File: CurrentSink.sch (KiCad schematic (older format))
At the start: 12 parts

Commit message: Updating the Schematic
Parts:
- removed U?: MIC5205-2.5YM5, Package_TO_SOT_SMD:SOT-23-5, symbol Regulator_Linear:MIC5205-2.5YM5
- added R? (x2): 10K, symbol Device:R
- added U?: TPS7A2401, symbol CurrentSink:TPS7A2401
- C?: value C -> 10uF
- C?: value C -> 1uF
- Q?: value Q_NMOS_DSG -> STP55NF06L; footprint (none) -> Package_TO_SOT_THT:TO-220-3_Vertical; MPN (none) -> STP55NF06L
- R?: value R -> 0.1
- U?: value MCP6002-xSN -> MCP6002; footprint (none) -> Package_SO:SOIC-8_3.9x4.9mm_P1.27mm; MPN (none) -> MCP6002T-I/SN
- U? (x2): value MCP6002-xSN -> MCP6002; footprint (none) -> Package_SO:SOIC-8_3.9x4.9mm_P1.27mm
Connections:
- wire segments 46 -> 57
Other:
- moved on the sheet: C?, U?C
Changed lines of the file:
@@
 P 5000 2650
 F 0 "U?" H 5000 3017 50  0000 C CNN
-F 1 "MCP6002-xSN" H 5000 2926 50  0000 C CNN
-F 2 "" H 5000 2650 50  0001 C CNN
+F 1 "MCP6002" H 5000 2926 50  0000 C CNN
+F 2 "Package_SO:SOIC-8_3.9x4.9mm_P1.27mm" H 5000 2650 50  0001 C CNN
 F 3 "http://ww1.microchip.com/downloads/en/DeviceDoc/21733j.pdf" H 5000 2650 50  0001 C CNN
+F 4 "MCP6002T-I/SN" H 5000 2650 50  0001 C CNN "MPN"
 	1    5000 2650
 	1    0    0    -1
@@
 L Amplifier_Operational:MCP6002-xSN U?
 U 3 1 6008AAAD
-P 8700 1450
-F 0 "U?" H 8658 1496 50  0000 L CNN
-F 1 "MCP6002-xSN" H 8658 1405 50  0000 L CNN
-F 2 "" H 8700 1450 50  0001 C CNN
-F 3 "http://ww1.microchip.com/downloads/en/DeviceDoc/21733j.pdf" H 8700 1450 50  0001 C CNN
-	3    8700 1450
+P 9100 1500
+F 0 "U?" H 9058 1546 50  0000 L CNN
+F 1 "MCP6002" H 9058 1455 50  0000 L CNN
+F 2 "Package_SO:SOIC-8_3.9x4.9mm_P1.27mm" H 9100 1500 50  0001 C CNN
+F 3 "http://ww1.microchip.com/downloads/en/DeviceDoc/21733j.pdf" H 9100 1500 50  0001 C CNN
+	3    9100 1500
 	1    0    0    -1
 $EndComp
@@
 P 2500 2850
 F 0 "U?" H 2500 3217 50  0000 C CNN
-F 1 "MCP6002-xSN" H 2500 3126 50  0000 C CNN
-F 2 "" H 2500 2850 50  0001 C CNN
+F 1 "MCP6002" H 2500 3126 50  0000 C CNN
+F 2 "Package_SO:SOIC-8_3.9x4.9mm_P1.27mm" H 2500 2850 50  0001 C CNN
 F 3 "http://ww1.microchip.com/downloads/en/DeviceDoc/21733j.pdf" H 2500 2850 50  0001 C CNN
 	2    2500 2850
-	1    0    0    -1
-$EndComp
-$Comp
-L Regulator_Linear:MIC5205-2.5YM5 U?
-U 1 1 60092225
-P 7450 1100
-F 0 "U?" H 7450 1442 50  0000 C CNN
-F 1 "MIC5205-2.5YM5" H 7450 1351 50  0000 C CNN
-F 2 "Package_TO_SOT_SMD:SOT-23-5" H 7450 1425 50  0001 C CNN
-F 3 "http://ww1.microchip.com/downloads/en/DeviceDoc/20005785A.pdf" H 7450 1100 50  0001 C CNN
-	1    7450 1100
 	1    0    0    -1
 $EndComp
@@
 P 6100 2650
 F 0 "Q?" H 6304 2696 50  0000 L CNN
-F 1 "Q_NMOS_DSG" H 6304 2605 50  0000 L CNN
-F 2 "" H 6300 2750 50  0001 C CNN
-F 3 "~" H 6100 2650 50  0001 C CNN
+F 1 "STP55NF06L" H 6304 2605 50  0000 L CNN
+F 2 "Package_TO_SOT_THT:TO-220-3_Vertical" H 6300 2750 50  0001 C CNN
+F 3 "https://www.st.com/content/ccc/resource/technical/document/datasheet/49/c5/a8/71/93/60/4f/86/CD00002690.pdf/files/CD00002690.pdf/jcr:content/translations/en.CD00002690.pdf" H 6100 2650 50  0001 C CNN
+F 4 "STP55NF06L" H 6100 2650 50  0001 C CNN "MPN"
 	1    6100 2650
 	1    0    0    -1
@@
 P 6200 3500
 F 0 "R?" H 6270 3546 50  0000 L CNN
-F 1 "R" H 6270 3455 50  0000 L CNN
+F 1 "0.1" H 6270 3455 50  0000 L CNN
 F 2 "" V 6130 3500 50  0001 C CNN
 F 3 "~" H 6200 3500 50  0001 C CNN
@@
 L Device:C C?
 U 1 1 600F940B
-P 8100 1300
-F 0 "C?" H 8215 1346 50  0000 L CNN
-F 1 "C" H 8215 1255 50  0000 L CNN
-F 2 "" H 8138 1150 50  0001 C CNN
-F 3 "~" H 8100 1300 50  0001 C CNN
-	1    8100 1300
+P 8550 1400
+F 0 "C?" H 8665 1446 50  0000 L CNN
+F 1 "10uF" H 8665 1355 50  0000 L CNN
+F 2 "" H 8588 1250 50  0001 C CNN
+F 3 "~" H 8550 1400 50  0001 C CNN
+	1    8550 1400
 	1    0    0    -1
 $EndComp
@@
 L Device:C C?
 U 1 1 600F9C77
-P 6750 1300
-F 0 "C?" H 6865 1346 50  0000 L CNN
-F 1 "C" H 6865 1255 50  0000 L CNN
-F 2 "" H 6788 1150 50  0001 C CNN
-F 3 "~" H 6750 1300 50  0001 C CNN
-	1    6750 1300
-	1    0    0    -1
-$EndComp
-Wire Wire Line
-	7750 1000 8100 1000
-Wire Wire Line
-	8600 1000 8600 1150
-Wire Wire Line
-	8100 1150 8100 1000
-Connection ~ 8100 1000
-Wire Wire Line
-	8100 1000 8600 1000
-Wire Wire Line
-	6750 1150 6750 1000
-Wire Wire Line
-	6750 1000 7150 1000
-Wire Wire Line
-	6750 1450 6750 1850
-Wire Wire Line
-	6750 1850 7450 1850
-Wire Wire Line
-	8600 1850 8600 1750
-Wire Wire Line
-	8100 1450 8100 1850
-Connection ~ 8100 1850
-Wire Wire Line
-	8100 1850 8600 1850
-Wire Wire Line
-	7450 1400 7450 1850
-Connection ~ 7450 1850
-Wire Wire Line
-	7450 1850 7750 1850
+P 6650 1400
+F 0 "C?" H 6765 1446 50  0000 L CNN
+F 1 "1uF" H 6765 1355 50  0000 L CNN
+F 2 "" H 6688 1250 50  0001 C CNN
+F 3 "~" H 6650 1400 50  0001 C CNN
+	1    6650 1400
+	1    0    0    -1
+$EndComp
 $Comp
 L power:GND #PWR?
 U 1 1 601192B6
-P 7750 2000
-F 0 "#PWR?" H 7750 1750 50  0001 C CNN
-F 1 "GND" H 7755 1827 50  0000 C CNN
-F 2 "" H 7750 2000 50  0001 C CNN
-F 3 "" H 7750 2000 50  0001 C CNN
-	1    7750 2000
-	1    0    0    -1
-$EndComp
-Wire Wire Line
-	7750 2000 7750 1850
-Connection ~ 7750 1850
-Wire Wire Line
-	7750 1850 8100 1850
+P 7500 2050
+F 0 "#PWR?" H 7500 1800 50  0001 C CNN
+F 1 "GND" H 7505 1877 50  0000 C CNN
+F 2 "" H 7500 2050 50  0001 C CNN
+F 3 "" H 7500 2050 50  0001 C CNN
+	1    7500 2050
+	1    0    0    -1
+$EndComp
 $Comp
 L Device:R_POT RV?
@@
 	6200 3650 6200 3950
 Wire Wire Line
-	6200 3950 4100 3950
+	6200 3950 5200 3950
 Text GLabel 4100 1850 1    50   Input ~ 0
 Vload
-Text GLabel 6350 1000 0    50   Input ~ 0
+Text GLabel 6500 950  0    50   Input ~ 0
 Vload
 Wire Wire Line
-	6350 1000 6750 1000
-Connection ~ 6750 1000
-Wire Wire Line
 	4100 1850 4100 2500
-Text GLabel 8850 1000 2    50   Input ~ 0
+Text GLabel 9250 950  2    50   Input ~ 0
 Vcc
-Wire Wire Line
-	8850 1000 8600 1000
-Connection ~ 8600 1000
 Text GLabel 1850 1950 1    50   Input ~ 0
 Vcc
@@
 	1    0    0    -1
 $EndComp
+$Comp
+L power:GND #PWR?
+U 1 1 600A09A2
+P 5200 4050
+F 0 "#PWR?" H 5200 3800 50  0001 C CNN
+F 1 "GND" H 5205 3877 50  0000 C CNN
+F 2 "" H 5200 4050 50  0001 C CNN
+F 3 "" H 5200 4050 50  0001 C CNN
+	1    5200 4050
+	1    0    0    -1
+$EndComp
+Wire Wire Line
+	5200 4050 5200 3950
+Connection ~ 5200 3950
+Wire Wire Line
+	5200 3950 4100 3950
+$Comp
+L CurrentSink:TPS7A2401 U?
+U 1 1 600F4C8B
+P 7500 1300
+F 0 "U?" H 7500 1915 50  0000 C CNN
+F 1 "TPS7A2401" H 7500 1824 50  0000 C CNN
+F 2 "" H 7500 1300 50  0001 C CNN
+F 3 "" H 7500 1300 50  0001 C CNN
+	1    7500 1300
+	1    0    0    -1
+$EndComp
+Wire Wire Line
+	6500 950  6650 950
+Wire Wire Line
+	6650 1250 6650 950
+Connection ~ 6650 950
+Wire Wire Line
+	6650 950  6900 950
+Wire Wire Line
+	7000 1100 6900 1100
+Wire Wire Line
+	6900 1100 6900 950
+Connection ~ 6900 950
+Wire Wire Line
+	6900 950  7000 950
+Wire Wire Line
+	6650 1550 6650 2000
+Wire Wire Line
+	6650 2000 7500 2000
+Wire Wire Line
+	7500 2000 7500 1850
+Wire Wire Line
+	7500 2050 7500 2000
+Connection ~ 7500 2000
+Wire Wire Line
+	8000 950  8200 950
+Wire Wire Line
+	9000 1200 9000 950
+Connection ~ 9000 950
+Wire Wire Line
+	9000 950  9250 950
+Wire Wire Line
+	8550 1250 8550 950
+Connection ~ 8550 950
+Wire Wire Line
+	8550 950  9000 950
+$Comp
+L Device:R R?
+U 1 1 600FFFE5
+P 8200 1150
+F 0 "R?" H 8270 1196 50  0000 L CNN
+F 1 "10K" H 8270 1105 50  0000 L CNN
+F 2 "" V 8130 1150 50  0001 C CNN
+F 3 "~" H 8200 1150 50  0001 C CNN
+	1    8200 1150
+	1    0    0    -1
+$EndComp
+$Comp
+L Device:R R?
+U 1 1 601007C4
+P 8200 1650
+F 0 "R?" H 8270 1696 50  0000 L CNN
+F 1 "10K" H 8270 1605 50  0000 L CNN
+F 2 "" V 8130 1650 50  0001 C CNN
+F 3 "~" H 8200 1650 50  0001 C CNN
+	1    8200 1650
+	1    0    0    -1
+$EndComp
+Wire Wire Line
+	8200 1000 8200 950
+Connection ~ 8200 950
+Wire Wire Line
+	8200 950  8550 950
+Wire Wire Line
+	8200 1300 8200 1400
+Wire Wire Line
+	8200 1800 8200 2000
+Wire Wire Line
+	8200 2000 7500 2000
+Wire Wire Line
+	8000 1400 8200 1400
+Connection ~ 8200 1400
+Wire Wire Line
+	8200 1400 8200 1500
+Wire Wire Line
+	9000 1800 9000 2000
+Wire Wire Line
+	9000 2000 8550 2000
+Connection ~ 8200 2000
+Wire Wire Line
+	8550 1550 8550 2000
+Connection ~ 8550 2000
+Wire Wire Line
+	8550 2000 8200 2000
 $EndSCHEMATC

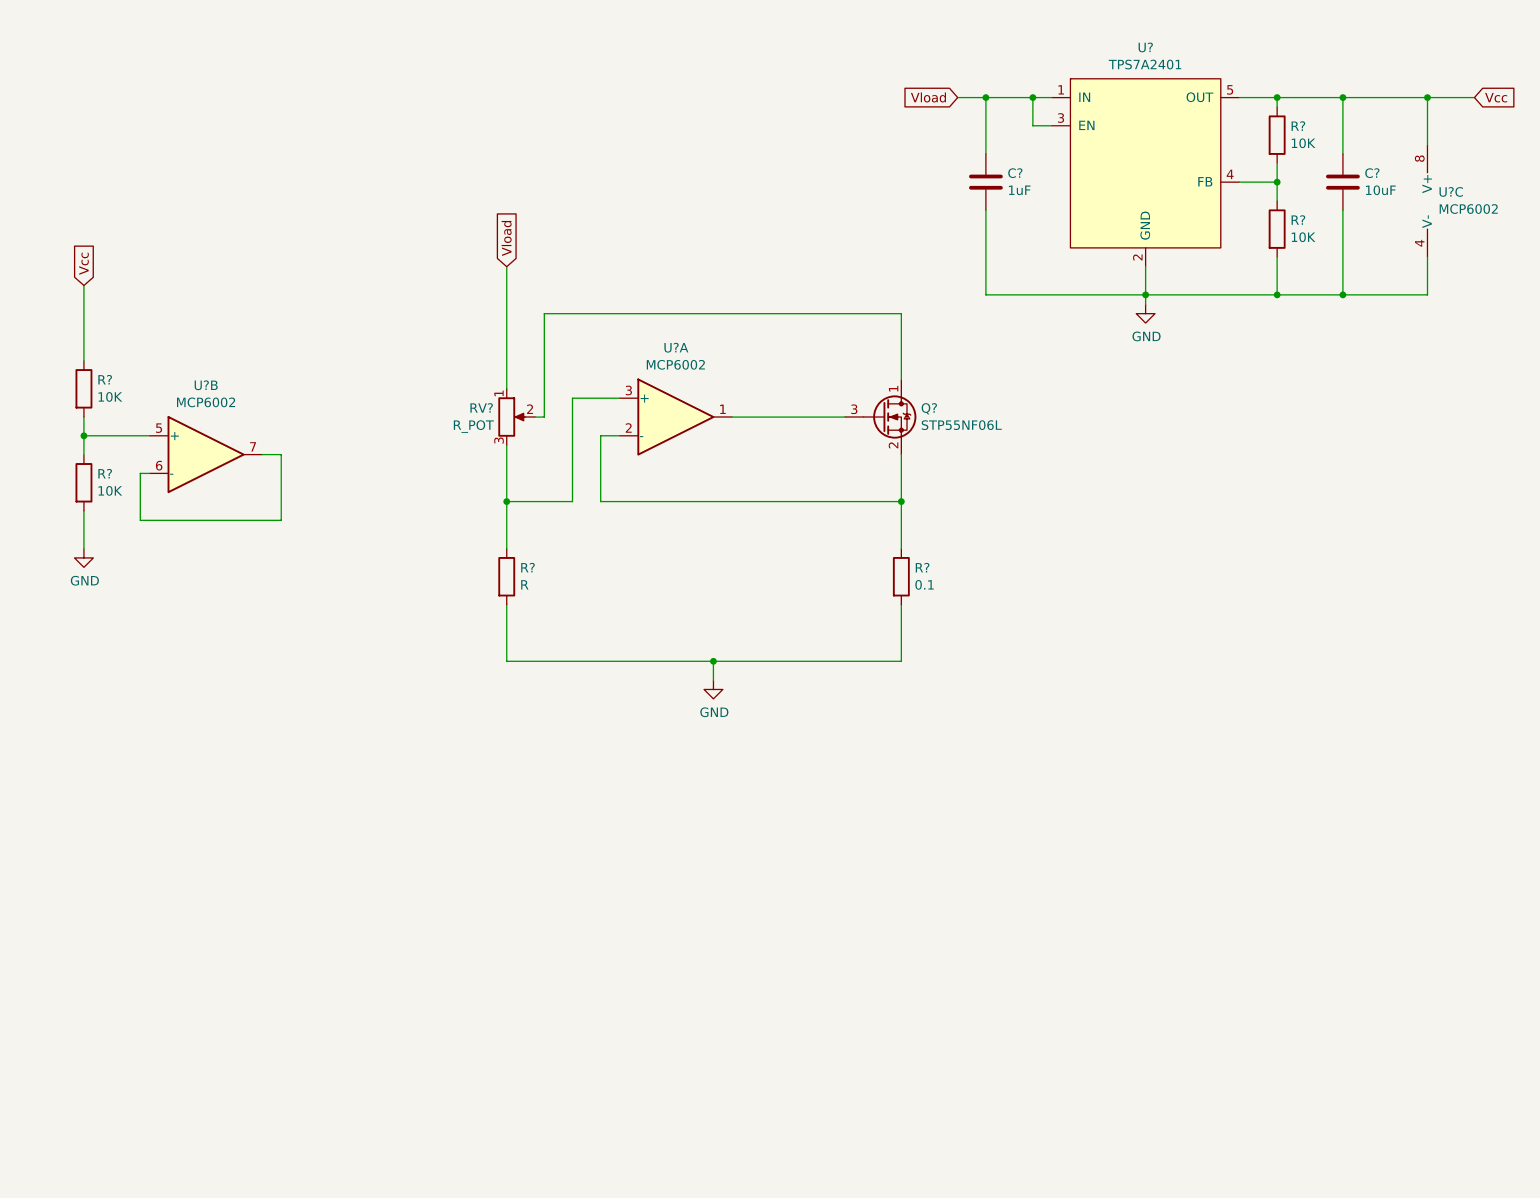
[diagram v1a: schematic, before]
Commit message: Schematic final version and preliminary footprints
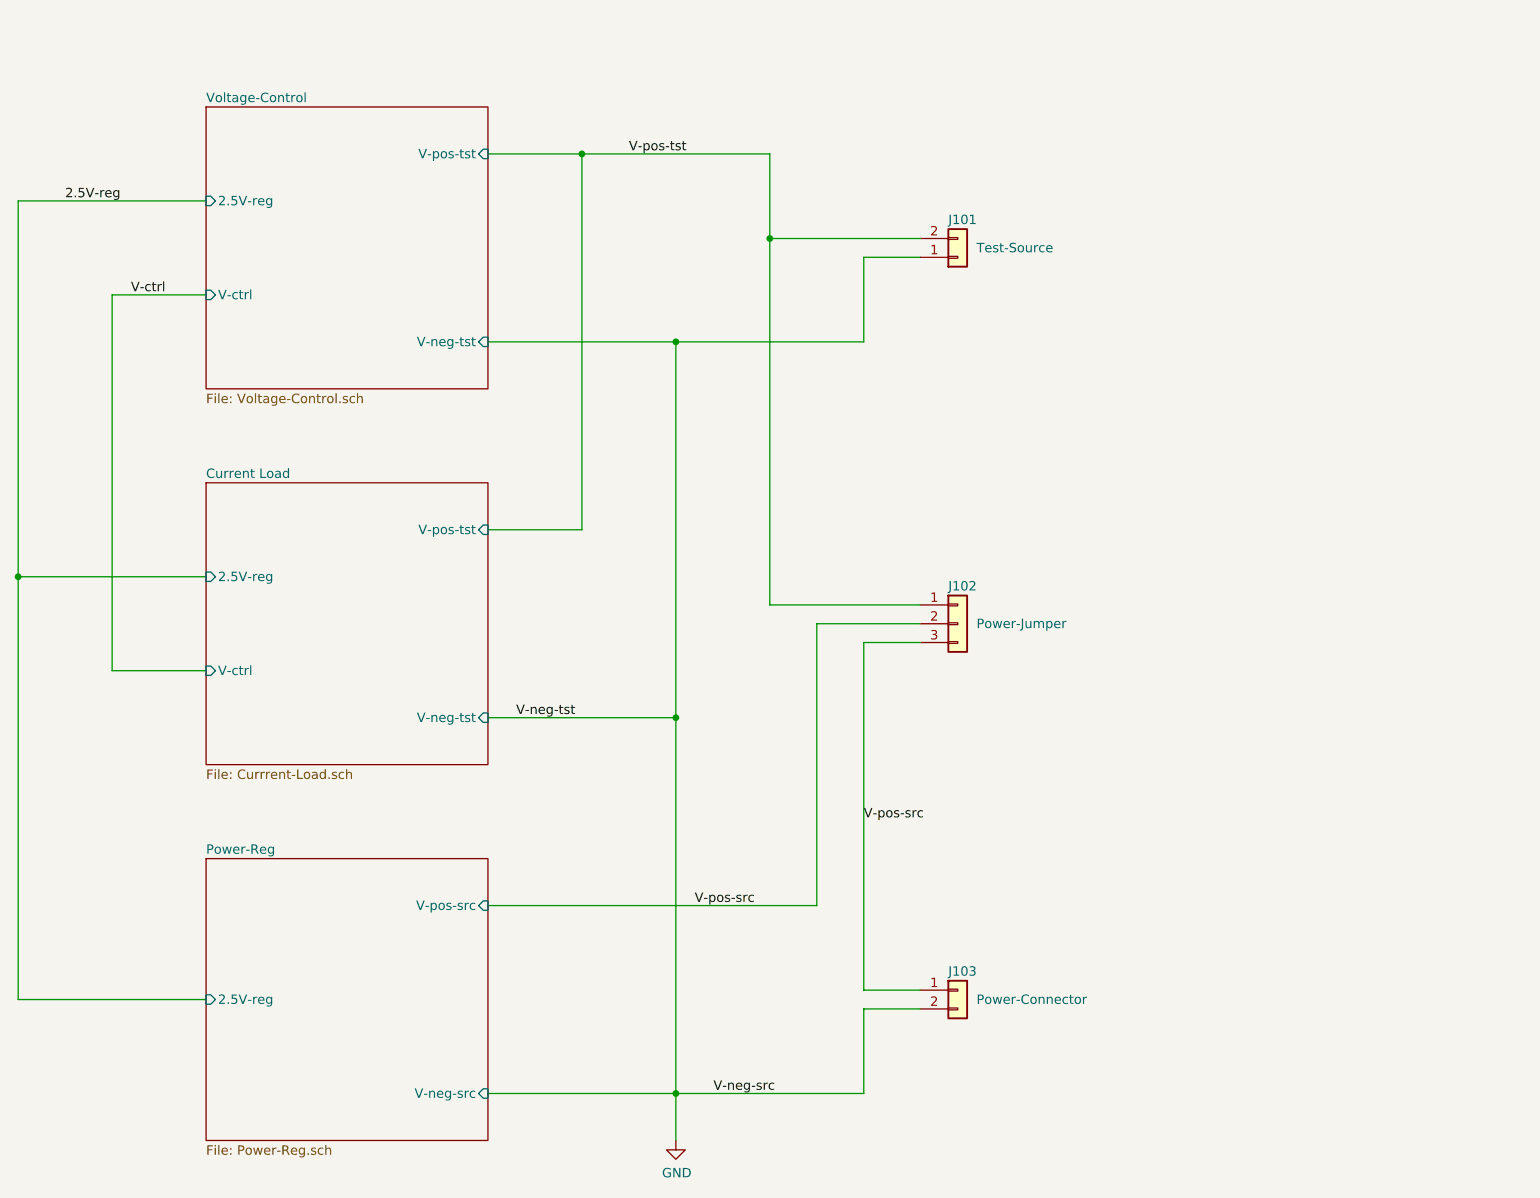
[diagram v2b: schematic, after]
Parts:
- removed C?: 10uF, symbol Device:C
- removed C?: 1uF, symbol Device:C
- removed Q?: STP55NF06L, Package_TO_SOT_THT:TO-220-3_Vertical, symbol Device:Q_NMOS_DSG
- removed R?: 0.1, symbol Device:R
- removed R?: R, symbol Device:R
- removed R? (x4): 10K, symbol Device:R
- removed RV?: R_POT, symbol Device:R_POT
- removed U? (x3): MCP6002, Package_SO:SOIC-8_3.9x4.9mm_P1.27mm, symbol Amplifier_Operational:MCP6002-xSN
- removed U?: TPS7A2401, symbol CurrentSink:TPS7A2401
- added J101: Test-Source, Connector_PinHeader_1.27mm:PinHeader_1x02_P1.27mm_Vertical, symbol Connector_Generic:Conn_01x02
- added J102: Power-Jumper, Connector_PinHeader_1.27mm:PinHeader_1x03_P1.27mm_Vertical, symbol Connector_Generic:Conn_01x03
- added J103: Power-Connector, Connector_BarrelJack:BarrelJack_CUI_PJ-036AH-SMT_Horizontal, symbol Connector_Generic:Conn_01x02
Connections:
- net GND: now also J101.1 (Pin_1), J103.2 (Pin_2)
- new net V-pos-src: J102.2 (Pin_2), J102.3 (Pin_3), J103.1 (Pin_1)
- new net V-pos-tst: J101.2 (Pin_2), J102.1 (Pin_1)
